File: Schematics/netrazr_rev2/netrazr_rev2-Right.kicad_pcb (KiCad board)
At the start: 2 copper layers, 167.6 x 119.4 mm, 79 parts, among them K10 *,,f8,,,,,,,8, K11 (,,f9,,,,,,,9, K12 ),,f10,,,,,,,0, K13 _,,f11,,,,,,,-, K14 +,,f12,,,,,,,=, K15 BKSP, K23 Y, K24 U, K25 I, K26 O, K27 P, K28 {,,,,,,,,,[}, K29 },,,,,,,,,], K30 |,,,,,,,,,\, K38 H, K39 J, K40 K, K41 L, K42 :,,,,,,,,,;, K43 ",,,,,,,,,', K44 ,,ENTER, K52 N, K53 M, K54 <,,,,,,,,,,, K55 >,,,,,,,,,., K56 ?,,,,,,,,,/, K57 RSHIFT, K58 UP, K59 DEL, K66 RSPACE, K67 RALT, K68 RCTRL, K69 LEFT, K70 DOWN, K71 RIGHT, K8 ^,,f6,,,,,,,6, K9 &,,f7,,,,,,,7

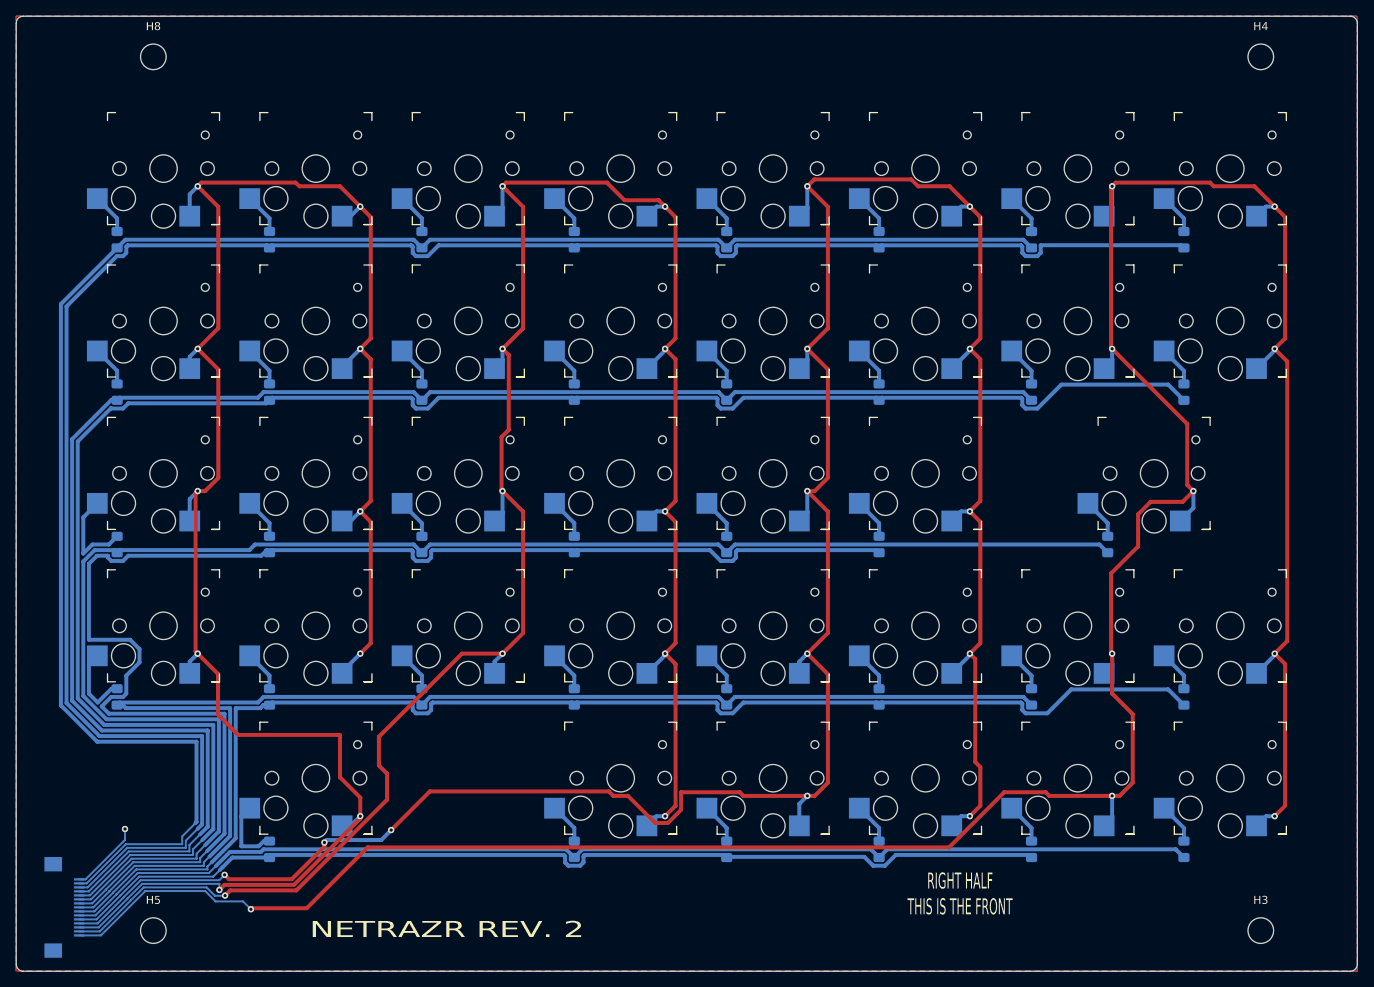
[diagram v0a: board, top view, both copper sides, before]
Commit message: fix PCB Mount placement, updated 3d model
fixed the size and placement of the mounting holes.

updated the 3d model of the pcb to better plan component spacing.

todo: add support columns to 3d model to support bolts, figure out how case will disassemble.
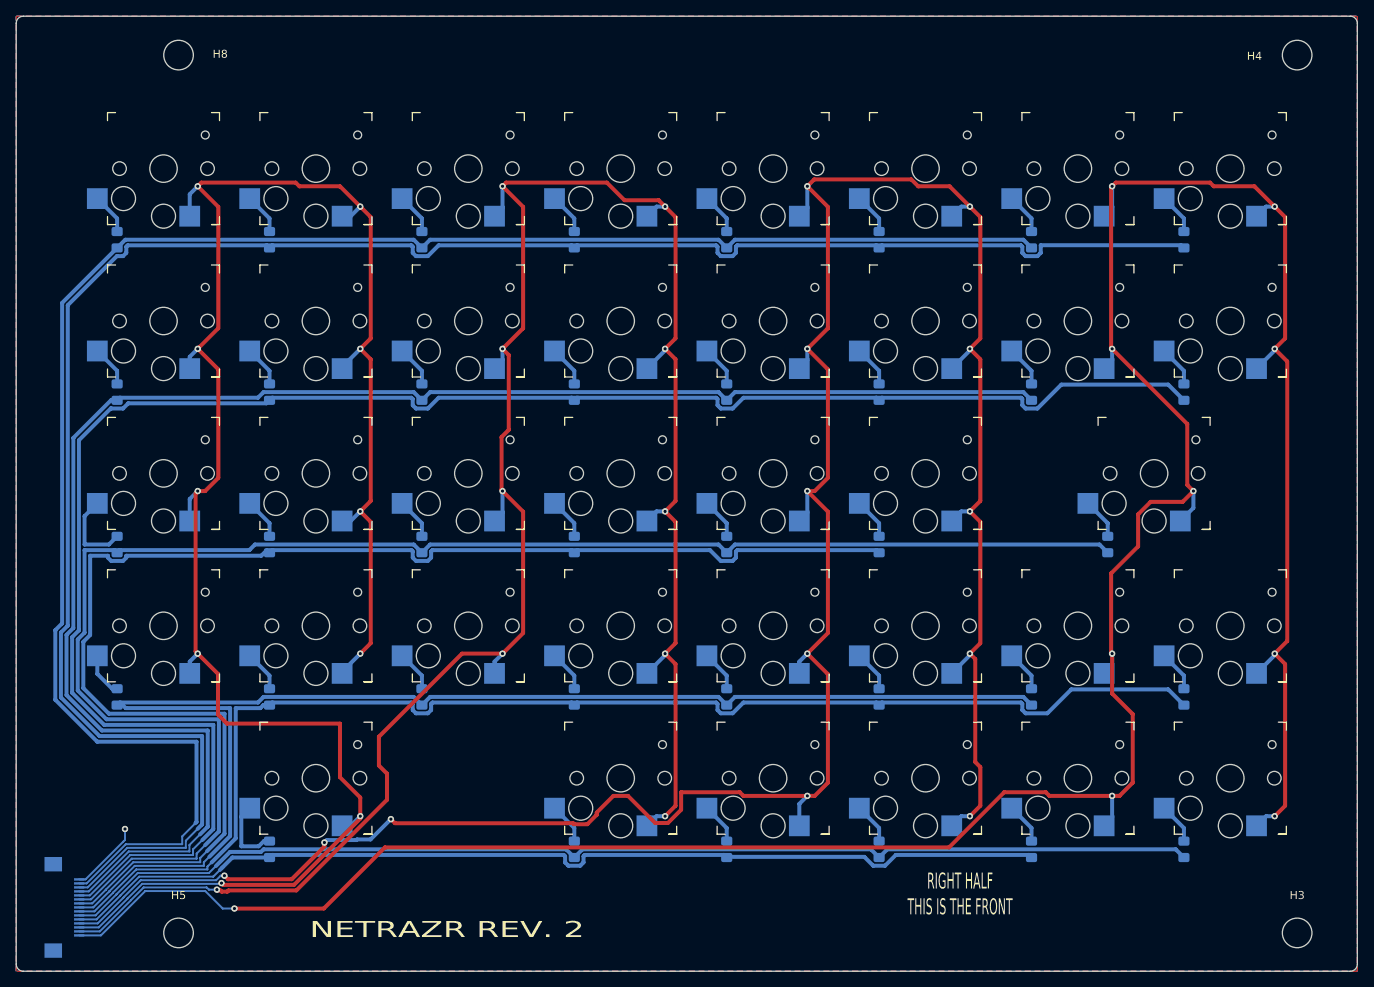
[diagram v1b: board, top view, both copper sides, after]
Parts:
- H3, H4, H5, H8: footprint MountingHole:MountingHole_3.2mm_M3_DIN965 -> MountingHole:MountingHole_3.7mm
- moved H3 4.55 mm to (375.9, 174.0)
- moved H4 4.55 mm to (375.9, 64.3)
- moved H5 3.16 mm to (236.1, 174.0)
- moved H8 3.16 mm to (236.1, 64.3)
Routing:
- net /Row_7: track 183.1 -> 176.5 mm
- net Net-(D52-Pad2): track 9.87 -> 5.50 mm
- net Net-(D38-Pad2): track 12.1 -> 10.3 mm
- net /Row_2: track 201.7 -> 203.0 mm
- net /Row_5: track 248.5 -> 249.1 mm
- net /Row_3: track 207.6 -> 208.2 mm
- net /Row_4: track 224.2 -> 224.8 mm
- net /Row_6: track 231.4 -> 232.0 mm
